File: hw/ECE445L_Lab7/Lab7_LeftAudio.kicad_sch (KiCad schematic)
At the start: 60 parts, among them Q10 PZT2222A, Q11 PZT2222A, Q12 PZT2222A, Q13 PZT2222A, Q14 PZT2222A, Q15 PZT2222A, Q16 PZT2222A, Q17 PZT2222A, Q18 PZT2222A, U11 OPA2350, U12 OPA2350, U13 OPA2350, U15 TLV5616, U6 OPA2350

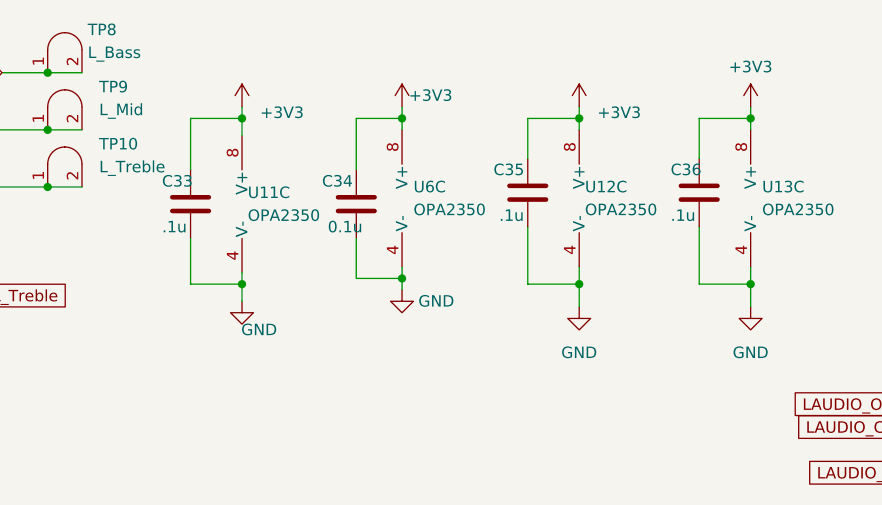
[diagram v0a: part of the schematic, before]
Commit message: Made changers to the schematic, updated bom, and created priliminary layout for the PCB. Ready for 7B Prep!
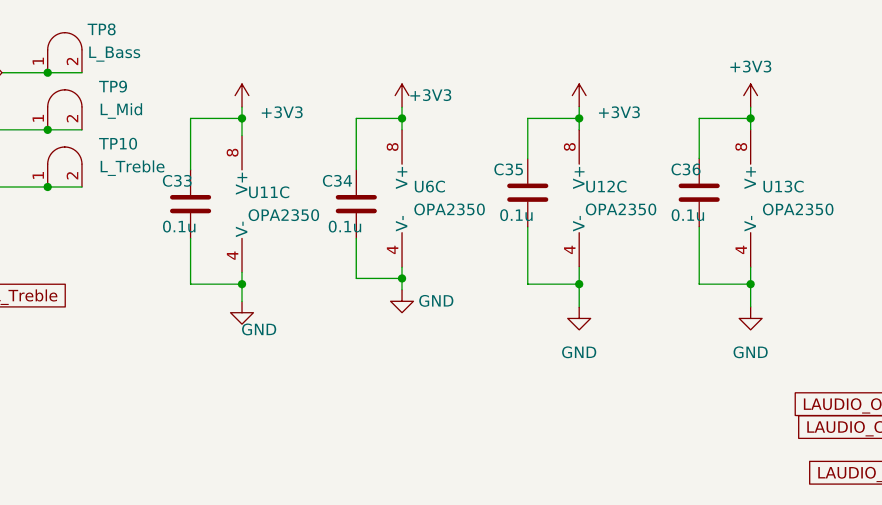
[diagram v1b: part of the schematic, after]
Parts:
- C27, C28, C29, C30, C31, C32, C34: footprint Capacitor_SMD:C_0805_2012Metric -> Capacitor_SMD:C_0603_1608Metric
- C33, C35, C36: value .1u -> 0.1u; footprint Capacitor_SMD:C_0805_2012Metric -> Capacitor_SMD:C_0603_1608Metric
- C37: footprint ECE445L:C_Axial_200mil -> Capacitor_SMD:C_0603_1608Metric
- R29, R30, R31, R32, R33, R34, R35, R36, R37, R38, R39, R40, R41, R42, R43, R44, R45, R46, R47, R48, R49, R50, R51, R52, R53, R54, R55, R56, R57: footprint Resistor_SMD:R_0805_2012Metric -> Resistor_SMD:R_0603_1608Metric
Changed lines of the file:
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@@
 			)
 		)
-		(property "Footprint" "Capacitor_SMD:C_0805_2012Metric"
+		(property "Footprint" "Capacitor_SMD:C_0603_1608Metric"
 			(at 42.545 37.7698 0)
 			(effects
@@
 			)
 		)
-		(property "Footprint" "Resistor_SMD:R_0805_2012Metric"
+		(property "Footprint" "Resistor_SMD:R_0603_1608Metric"
 			(at 50.292 170.815 90)
 			(effects
@@
 			)
 		)
-		(property "Footprint" "Capacitor_SMD:C_0805_2012Metric"
+		(property "Footprint" "Capacitor_SMD:C_0603_1608Metric"
 			(at 146.9898 29.845 0)
 			(effects
@@
 			)
 		)
-		(property "Footprint" "Resistor_SMD:R_0805_2012Metric"
+		(property "Footprint" "Resistor_SMD:R_0603_1608Metric"
 			(at 45.593 52.07 90)
 			(effects
@@
 			)
 		)
-		(property "Footprint" "Resistor_SMD:R_0805_2012Metric"
+		(property "Footprint" "Resistor_SMD:R_0603_1608Metric"
 			(at 245.237 151.13 90)
 			(effects
@@
 			)
 		)
-		(property "Footprint" "Resistor_SMD:R_0805_2012Metric"
+		(property "Footprint" "Resistor_SMD:R_0603_1608Metric"
 			(at 89.027 111.76 90)
 			(effects
@@
 			)
 		)
-		(property "Footprint" "Resistor_SMD:R_0805_2012Metric"
+		(property "Footprint" "Resistor_SMD:R_0603_1608Metric"
 			(at 173.355 124.333 90)
 			(effects
@@
 			)
 		)
-		(property "Value" ".1u"
+		(property "Value" "0.1u"
 			(at 126.365 36.195 0)
 			(effects
@@
 			)
 		)
-		(property "Footprint" "Capacitor_SMD:C_0805_2012Metric"
+		(property "Footprint" "Capacitor_SMD:C_0603_1608Metric"
 			(at 128.5748 29.845 0)
 			(effects
@@
 			)
 		)
-		(property "Footprint" "Resistor_SMD:R_0805_2012Metric"
+		(property "Footprint" "Resistor_SMD:R_0603_1608Metric"
 			(at 241.427 151.13 90)
 			(effects
@@
 			)
 		)
-		(property "Footprint" "Resistor_SMD:R_0805_2012Metric"
+		(property "Footprint" "Resistor_SMD:R_0603_1608Metric"
 			(at 39.37 154.178 90)
 			(effects
@@
 			)
 		)
-		(property "Footprint" "Resistor_SMD:R_0805_2012Metric"
+		(property "Footprint" "Resistor_SMD:R_0603_1608Metric"
 			(at 49.657 57.15 90)
 			(effects
@@
 			)
 		)
-		(property "Footprint" "Resistor_SMD:R_0805_2012Metric"
+		(property "Footprint" "Resistor_SMD:R_0603_1608Metric"
 			(at 45.593 33.655 90)
 			(effects
@@
 			)
 		)
-		(property "Footprint" "Resistor_SMD:R_0805_2012Metric"
+		(property "Footprint" "Resistor_SMD:R_0603_1608Metric"
 			(at 226.695 126.873 90)
 			(effects
@@
 			)
 		)
-		(property "Footprint" "Resistor_SMD:R_0805_2012Metric"
+		(property "Footprint" "Resistor_SMD:R_0603_1608Metric"
 			(at 67.31 166.243 90)
 			(effects
@@
 			)
 		)
-		(property "Footprint" "Resistor_SMD:R_0805_2012Metric"
+		(property "Footprint" "Resistor_SMD:R_0603_1608Metric"
 			(at 27.305 150.622 90)
 			(effects
@@
 			)
 		)
-		(property "Footprint" "Resistor_SMD:R_0805_2012Metric"
+		(property "Footprint" "Resistor_SMD:R_0603_1608Metric"
 			(at 60.198 170.815 90)
 			(effects
@@
 			)
 		)
-		(property "Footprint" "Resistor_SMD:R_0805_2012Metric"
+		(property "Footprint" "Resistor_SMD:R_0603_1608Metric"
 			(at 84.328 99.06 90)
 			(effects
@@
 			)
 		)
-		(property "Footprint" "Resistor_SMD:R_0805_2012Metric"
+		(property "Footprint" "Resistor_SMD:R_0603_1608Metric"
 			(at 231.775 111.252 90)
 			(effects
@@
 			)
 		)
-		(property "Footprint" "Resistor_SMD:R_0805_2012Metric"
+		(property "Footprint" "Resistor_SMD:R_0603_1608Metric"
 			(at 59.563 57.15 90)
 			(effects
@@
 			)
 		)
-		(property "Footprint" "Resistor_SMD:R_0805_2012Metric"
+		(property "Footprint" "Resistor_SMD:R_0603_1608Metric"
 			(at 226.568 106.68 90)
 			(effects
@@
 			)
 		)
-		(property "Footprint" "Resistor_SMD:R_0805_2012Metric"
+		(property "Footprint" "Resistor_SMD:R_0603_1608Metric"
 			(at 98.933 111.76 90)
 			(effects
@@
 			)
 		)
-		(property "Footprint" "Resistor_SMD:R_0805_2012Metric"
+		(property "Footprint" "Resistor_SMD:R_0603_1608Metric"
 			(at 268.097 151.13 90)
 			(effects
@@
 			)
 		)
-		(property "Footprint" "Resistor_SMD:R_0805_2012Metric"
+		(property "Footprint" "Resistor_SMD:R_0603_1608Metric"
 			(at 217.678 106.045 90)
 			(effects
@@
 			)
 		)
-		(property "Footprint" "Resistor_SMD:R_0805_2012Metric"
+		(property "Footprint" "Resistor_SMD:R_0603_1608Metric"
 			(at 256.032 151.13 90)
 			(effects
@@
 			)
 		)
-		(property "Footprint" "ECE445L:C_Axial_200mil"
+		(property "Footprint" "Capacitor_SMD:C_0603_1608Metric"
 			(at 261.9502 52.07 0)
 			(effects
@@
 			)
 		)
-		(property "Footprint" "Resistor_SMD:R_0805_2012Metric"
+		(property "Footprint" "Resistor_SMD:R_0603_1608Metric"
 			(at 106.045 107.188 90)
 			(effects
@@
 			)
 		)
-		(property "Footprint" "Resistor_SMD:R_0805_2012Metric"
+		(property "Footprint" "Resistor_SMD:R_0603_1608Metric"
 			(at 66.675 52.578 90)
 			(effects
@@
 			)
 		)
-		(property "Footprint" "Resistor_SMD:R_0805_2012Metric"
+		(property "Footprint" "Resistor_SMD:R_0603_1608Metric"
 			(at 173.355 135.128 90)
 			(effects
@@
 			)
 		)
-		(property "Footprint" "Resistor_SMD:R_0805_2012Metric"
+		(property "Footprint" "Resistor_SMD:R_0603_1608Metric"
 			(at 29.972 27.94 90)
 			(effects
@@
 			)
 		)
-		(property "Footprint" "Capacitor_SMD:C_0805_2012Metric"
+		(property "Footprint" "Capacitor_SMD:C_0603_1608Metric"
 			(at 124.1298 98.425 0)
 			(effects
@@
 			)
 		)
-		(property "Value" ".1u"
+		(property "Value" "0.1u"
 			(at 163.83 34.925 0)
 			(effects
@@
 			)
 		)
-		(property "Footprint" "Capacitor_SMD:C_0805_2012Metric"
+		(property "Footprint" "Capacitor_SMD:C_0603_1608Metric"
 			(at 166.0398 28.575 0)
 			(effects
@@
 			)
 		)
-		(property "Footprint" "Capacitor_SMD:C_0805_2012Metric"
+		(property "Footprint" "Capacitor_SMD:C_0603_1608Metric"
 			(at 30.48 37.7698 0)
 			(effects
@@
 			)
 		)
-		(property "Footprint" "Capacitor_SMD:C_0805_2012Metric"
+		(property "Footprint" "Capacitor_SMD:C_0603_1608Metric"
 			(at 78.74 91.7448 0)
 			(effects
@@
 			)
 		)
-		(property "Footprint" "Resistor_SMD:R_0805_2012Metric"
+		(property "Footprint" "Resistor_SMD:R_0603_1608Metric"
 			(at 173.99 113.538 90)
 			(effects
@@
 			)
 		)
-		(property "Footprint" "Capacitor_SMD:C_0805_2012Metric"
+		(property "Footprint" "Capacitor_SMD:C_0603_1608Metric"
 			(at 34.6202 147.32 0)
 			(effects
@@
 			)
 		)
-		(property "Footprint" "Resistor_SMD:R_0805_2012Metric"
+		(property "Footprint" "Resistor_SMD:R_0603_1608Metric"
 			(at 84.328 87.63 90)
 			(effects
@@
 			)
 		)
-		(property "Footprint" "Resistor_SMD:R_0805_2012Metric"
+		(property "Footprint" "Resistor_SMD:R_0603_1608Metric"
 			(at 117.475 97.028 90)
 			(effects
@@
 			)
 		)
-		(property "Footprint" "Resistor_SMD:R_0805_2012Metric"
+		(property "Footprint" "Resistor_SMD:R_0603_1608Metric"
 			(at 217.678 135.255 90)
 			(effects
@@
 			)
 		)
-		(property "Value" ".1u"
+		(property "Value" "0.1u"
 			(at 182.88 34.925 0)
 			(effects
@@
 			)
 		)
-		(property "Footprint" "Capacitor_SMD:C_0805_2012Metric"
+		(property "Footprint" "Capacitor_SMD:C_0603_1608Metric"
 			(at 185.0898 28.575 0)
 			(effects
@@
 			)
 		)
-		(property "Footprint" "Capacitor_SMD:C_0805_2012Metric"
+		(property "Footprint" "Capacitor_SMD:C_0603_1608Metric"
 			(at 45.4152 169.545 0)
 			(effects

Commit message: Rough draft layout - need to remove tm4c chip
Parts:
- removed TP10: L_Treble, ECE445L:Testpoint_1x02_P2.54mm, symbol ECE445L:Testpoint
- removed TP11: L_Buff, ECE445L:Testpoint_1x02_P2.54mm, symbol ECE445L:Testpoint
- removed TP12: L_Out, ECE445L:Testpoint_1x02_P2.54mm, symbol ECE445L:Testpoint
- removed TP8: L_Bass, ECE445L:Testpoint_1x02_P2.54mm, symbol ECE445L:Testpoint
- removed TP9: L_Mid, ECE445L:Testpoint_1x02_P2.54mm, symbol ECE445L:Testpoint
- added R59: 40k, Resistor_SMD:R_0603_1608Metric_Pad0.98x0.95mm_HandSolder, symbol Device:R
- added R60: 3.3k, Resistor_SMD:R_0603_1608Metric_Pad0.98x0.95mm_HandSolder, symbol Device:R
- C27: renamed from C31; footprint Capacitor_SMD:C_0603_1608Metric -> Capacitor_SMD:C_0603_1608Metric_Pad1.08x0.95mm_HandSolder
- C28: renamed from C27; value 27n -> 30n; footprint Capacitor_SMD:C_0603_1608Metric -> Capacitor_SMD:C_0603_1608Metric_Pad1.08x0.95mm_HandSolder
- C29: renamed from C32; footprint Capacitor_SMD:C_0603_1608Metric -> Capacitor_SMD:C_0603_1608Metric_Pad1.08x0.95mm_HandSolder
- C30: renamed from C28; value 27n -> 30n; footprint Capacitor_SMD:C_0603_1608Metric -> Capacitor_SMD:C_0603_1608Metric_Pad1.08x0.95mm_HandSolder
- C31: renamed from C29; value 10n -> 9.5n; footprint Capacitor_SMD:C_0603_1608Metric -> Capacitor_SMD:C_0603_1608Metric_Pad1.08x0.95mm_HandSolder
- C32: renamed from C30; value 3.5n -> 3.7n; footprint Capacitor_SMD:C_0603_1608Metric -> Capacitor_SMD:C_0603_1608Metric_Pad1.08x0.95mm_HandSolder
- C33, C34, C35, C36: footprint Capacitor_SMD:C_0603_1608Metric -> Capacitor_SMD:C_0603_1608Metric_Pad1.08x0.95mm_HandSolder
- C37: renamed from C40; footprint Capacitor_SMD:C_0805_2012Metric -> Capacitor_SMD:C_0805_2012Metric_Pad1.18x1.45mm_HandSolder
- C38: renamed from C37; footprint Capacitor_SMD:C_0603_1608Metric -> Capacitor_SMD:C_0603_1608Metric_Pad1.08x0.95mm_HandSolder
- R39: renamed from R29; footprint Resistor_SMD:R_0603_1608Metric -> Resistor_SMD:R_0603_1608Metric_Pad0.98x0.95mm_HandSolder
- R40: footprint Resistor_SMD:R_0603_1608Metric -> Resistor_SMD:R_0603_1608Metric_Pad0.98x0.95mm_HandSolder
- R41: renamed from R30; footprint Resistor_SMD:R_0603_1608Metric -> Resistor_SMD:R_0603_1608Metric_Pad0.98x0.95mm_HandSolder
- R42: renamed from R43; footprint Resistor_SMD:R_0603_1608Metric -> Resistor_SMD:R_0603_1608Metric_Pad0.98x0.95mm_HandSolder
- R43: renamed from R44; footprint Resistor_SMD:R_0603_1608Metric -> Resistor_SMD:R_0603_1608Metric_Pad0.98x0.95mm_HandSolder
- R44: renamed from R45; footprint Resistor_SMD:R_0603_1608Metric -> Resistor_SMD:R_0603_1608Metric_Pad0.98x0.95mm_HandSolder
- R45: renamed from R33; footprint Resistor_SMD:R_0603_1608Metric -> Resistor_SMD:R_0603_1608Metric_Pad0.98x0.95mm_HandSolder
- R46: renamed from R42; footprint Resistor_SMD:R_0603_1608Metric -> Resistor_SMD:R_0603_1608Metric_Pad0.98x0.95mm_HandSolder
- R47: renamed from R32; footprint Resistor_SMD:R_0603_1608Metric -> Resistor_SMD:R_0603_1608Metric_Pad0.98x0.95mm_HandSolder
- R48: renamed from R41; footprint Resistor_SMD:R_0603_1608Metric -> Resistor_SMD:R_0603_1608Metric_Pad0.98x0.95mm_HandSolder
- R49: renamed from R31; footprint Resistor_SMD:R_0603_1608Metric -> Resistor_SMD:R_0603_1608Metric_Pad0.98x0.95mm_HandSolder
- R50: renamed from R34; footprint Resistor_SMD:R_0603_1608Metric -> Resistor_SMD:R_0603_1608Metric_Pad0.98x0.95mm_HandSolder
- R51: renamed from R35; footprint Resistor_SMD:R_0603_1608Metric -> Resistor_SMD:R_0603_1608Metric_Pad0.98x0.95mm_HandSolder
- R52: renamed from R39; footprint Resistor_SMD:R_0603_1608Metric -> Resistor_SMD:R_0603_1608Metric_Pad0.98x0.95mm_HandSolder
- R53: renamed from R38; footprint Resistor_SMD:R_0603_1608Metric -> Resistor_SMD:R_0603_1608Metric_Pad0.98x0.95mm_HandSolder
- R54: renamed from R37; footprint Resistor_SMD:R_0603_1608Metric -> Resistor_SMD:R_0603_1608Metric_Pad0.98x0.95mm_HandSolder
- R55: renamed from R36; footprint Resistor_SMD:R_0603_1608Metric -> Resistor_SMD:R_0603_1608Metric_Pad0.98x0.95mm_HandSolder
- R56: renamed from R47; value 10k -> 7.5k; footprint Resistor_SMD:R_0603_1608Metric -> Resistor_SMD:R_0603_1608Metric_Pad0.98x0.95mm_HandSolder
- R57: renamed from R48; footprint Resistor_SMD:R_0603_1608Metric -> Resistor_SMD:R_0603_1608Metric_Pad0.98x0.95mm_HandSolder
- R58: renamed from R46; footprint Resistor_SMD:R_0603_1608Metric -> Resistor_SMD:R_0603_1608Metric_Pad0.98x0.95mm_HandSolder
- R61: renamed from R49; footprint Resistor_SMD:R_0603_1608Metric -> Resistor_SMD:R_0603_1608Metric_Pad0.98x0.95mm_HandSolder
- R62: renamed from R50; footprint Resistor_SMD:R_0603_1608Metric -> Resistor_SMD:R_0603_1608Metric_Pad0.98x0.95mm_HandSolder
- R63: renamed from R52; footprint Resistor_SMD:R_0603_1608Metric -> Resistor_SMD:R_0603_1608Metric_Pad0.98x0.95mm_HandSolder
- R64: renamed from R51; footprint Resistor_SMD:R_0603_1608Metric -> Resistor_SMD:R_0603_1608Metric_Pad0.98x0.95mm_HandSolder
- R65: renamed from R53; footprint Resistor_SMD:R_0603_1608Metric -> Resistor_SMD:R_0603_1608Metric_Pad0.98x0.95mm_HandSolder
- R66: renamed from R54; footprint Resistor_SMD:R_0603_1608Metric -> Resistor_SMD:R_0603_1608Metric_Pad0.98x0.95mm_HandSolder
- R67: renamed from R55; footprint Resistor_SMD:R_0603_1608Metric -> Resistor_SMD:R_0603_1608Metric_Pad0.98x0.95mm_HandSolder
- R68: renamed from R57; footprint Resistor_SMD:R_0603_1608Metric -> Resistor_SMD:R_0603_1608Metric_Pad0.98x0.95mm_HandSolder
- R69: renamed from R56; footprint Resistor_SMD:R_0603_1608Metric -> Resistor_SMD:R_0603_1608Metric_Pad0.98x0.95mm_HandSolder
- renumbered U6 to U11, U6 to U12, U11 to U12, U12 to U13, U13 to U14
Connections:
- net R_Bass is gone; now on net L_Bass: R57.1
- net R_Mid is gone; now on net L_Mid: R56.1
- net R_Treble is gone; now on net L_Treble: R58.1
- net Vin is gone; now on net Vin_L: C27.1, C31.1
- net GND: now also R65.2, R59.1; no longer R65.1
- net L_Buff: now also R60.2; no longer U14.2 (-)
- net Vin_L: now also R39.1; no longer R39.2
- net at C28.2, R41.1: now also R39.2; no longer R39.1
- net at R50.1, R51.2: now also C31.2, U13.3 (+)
- net at R63.1, U14.5 (+): now also R65.1; no longer R65.2
- new net: R59.2, R60.1, U14.2 (-)
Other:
- company: (none) -> The University of Texas at Austin
- title: (none) -> ECE 445L Lab7
- moved on the sheet: R39, R65, U12B

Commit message: Added current consumption to schematic
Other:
- note added: "100k Ohm Resistor Dividers : 2 * (0.0165 mA) = 0.033 mA 200k Ohm Resistor Dividers : 1 * 0.00825 = 0.00825 mA 10k Ohm Resitor Dividers : 3 * (0.165 mA) = 0.5 mA 75k Ohm Loads : 1 * (0.044 mA) = 0.044 mA OPA2350s : 8 * (7.5 mA) = 60 mA TLV5616s : 1 * (1.1mA) = 1.1 mA Total : 61.6825 mA"
- note added: "Current per 100k Ohm Resitor Divider +3V3 / (100k + 100k) = 0.0165 mA Current per 200k Ohm Resistor Divider +3V3 / (200k + 200k) = 0.00825 mA Current per 10k Ohm Resitor Divider +3V3 / (10k + 10k) = 0.165 mA Current per 75k Load +3V3 / 75k = 0.044 mA Quiescent Current (Per Amplifier - 2x per chip) 7.5 mA Current Per TLV5616 1.1 mA"
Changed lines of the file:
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@@
+		)
+	)
+	(text "100k Ohm Resistor Dividers : 2 * (0.0165 mA) = 0.033 mA\n200k Ohm Resistor Dividers : 1 * 0.00825 = 0.00825 mA\n10k Ohm Resitor Dividers : 3 * (0.165 mA) = 0.5 mA\n75k Ohm Loads : 1 * (0.044 mA) = 0.044 mA\nOPA2350s : 8 * (7.5 mA) = 60 mA\nTLV5616s : 1 * (1.1mA) = 1.1 mA\n\nTotal : 61.6825 mA"
+		(exclude_from_sim no)
+		(at 117.475 185.42 0)
+		(effects
+			(font
+				(size 1.27 1.27)
+			)
+			(justify left)
 		)
 	)
@@
 		)
 	)
+	(text "Current per 100k Ohm Resitor Divider\n+3V3 / (100k + 100k) = 0.0165 mA\n\nCurrent per 200k Ohm Resistor Divider\n+3V3 / (200k + 200k) = 0.00825 mA\n\nCurrent per 10k Ohm Resitor Divider\n+3V3 / (10k + 10k) = 0.165 mA\n\nCurrent per 75k Load\n+3V3 / 75k = 0.044 mA\n\nQuiescent Current (Per Amplifier - 2x per chip)\n7.5 mA\n\nCurrent Per TLV5616\n1.1 mA\n"
+		(exclude_from_sim no)
+		(at 118.11 156.845 0)
+		(effects
+			(font
+				(size 1.27 1.27)
+			)
+			(justify left)
+		)
+	)

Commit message: Updated lab7a report
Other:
- note added: "Left Audio Current Consumption : Current per 100k Ohm Resitor Divider +3V3 / (100k + 100k) = 0.0165 mA Current per 200k Ohm Resistor Divider +3V3 / (200k + 200k) = 0.00825 mA Current per 10k Ohm Resitor Divider +3V3 / (10k + 10k) = 0.165 mA Current per 75k Load +3V3 / 75k = 0.044 mA Quiescent Current (Per Amplifier - 2x per chip) 7.5 mA Current Per TLV5616 1.1 mA"
- note removed: "Current per 100k Ohm Resitor Divider +3V3 / (100k + 100k) = 0.0165 mA Current per 200k Ohm Resistor Divider +3V3 / (200k + 200k) = 0.00825 mA Current per 10k Ohm Resitor Divider +3V3 / (10k + 10k) = 0.165 mA Current per 75k Load +3V3 / 75k = 0.044 mA Quiescent Current (Per Amplifier - 2x per chip) 7.5 mA Current Per TLV5616 1.1 mA"
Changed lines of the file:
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@@
 		)
 	)
-	(text "Current per 100k Ohm Resitor Divider\n+3V3 / (100k + 100k) = 0.0165 mA\n\nCurrent per 200k Ohm Resistor Divider\n+3V3 / (200k + 200k) = 0.00825 mA\n\nCurrent per 10k Ohm Resitor Divider\n+3V3 / (10k + 10k) = 0.165 mA\n\nCurrent per 75k Load\n+3V3 / 75k = 0.044 mA\n\nQuiescent Current (Per Amplifier - 2x per chip)\n7.5 mA\n\nCurrent Per TLV5616\n1.1 mA\n"
+	(text "Left Audio Current Consumption :\n\nCurrent per 100k Ohm Resitor Divider\n+3V3 / (100k + 100k) = 0.0165 mA\n\nCurrent per 200k Ohm Resistor Divider\n+3V3 / (200k + 200k) = 0.00825 mA\n\nCurrent per 10k Ohm Resitor Divider\n+3V3 / (10k + 10k) = 0.165 mA\n\nCurrent per 75k Load\n+3V3 / 75k = 0.044 mA\n\nQuiescent Current (Per Amplifier - 2x per chip)\n7.5 mA\n\nCurrent Per TLV5616\n1.1 mA\n"
 		(exclude_from_sim no)
 		(at 118.11 156.845 0)

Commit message: PCB Layout
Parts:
- added R105, R106, R107, R108, R109, R110, R111, R112, R113: 2k, Resistor_SMD:R_0603_1608Metric_Pad0.98x0.95mm_HandSolder, symbol Device:R
- added TP10: L_Bass, ECE445L:Testpoint_1x02_P2.54mm, symbol ECE445L:Testpoint
- added TP8: L_Treble, ECE445L:Testpoint_1x02_P2.54mm, symbol ECE445L:Testpoint
- added TP9: L_Mid, ECE445L:Testpoint_1x02_P2.54mm, symbol ECE445L:Testpoint
- Q10, Q11, Q12, Q13, Q14, Q15, Q16, Q17, Q18: value PZT2222A -> MMBF170; footprint Package_TO_SOT_SMD:SOT-223-3_TabPin2 -> Package_TO_SOT_SMD:SOT-23-3
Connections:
- net L_Bass: now also TP10.1 (A), TP10.2 (B)
- net L_Mid: now also TP9.1 (A), TP9.2 (B)
- net L_Treble: now also TP8.1 (A), TP8.2 (B)
- net PB2: now also R107.1; no longer Q11.1 (B)
- net PB3: now also R108.2; no longer Q13.1 (B)
- net PB4: now also R105.1; no longer Q14.1 (B)
- net PB5: now also R106.2; no longer Q15.1 (B)
- net PB6: now also R109.1; no longer Q10.1 (B)
- net PB7: now also R110.2; no longer Q12.1 (B)
- net PC4: now also R111.2; no longer Q16.1 (B)
- net PC5: now also R112.1; no longer Q17.1 (B)
- net PC6: now also R113.1; no longer Q18.1 (B)
- net at R45.1, R49.1, U12.2 (-): now also R47.1; no longer R47.2
- net at R52.1, R54.1, U13.2 (-): now also R53.1; no longer R53.2
- net at Q12.2 (C): now also R46.2; no longer R46.1
- net at R44.1, R48.1, U11.2 (-): now also R46.1; no longer R46.2
- net at Q13.2 (C): now also R47.2; no longer R47.1
- net at Q15.2 (C): now also R53.2; no longer R53.1
- new net: Q14.1 (B), R105.2
- new net: Q12.1 (B), R110.1
- new net: Q11.1 (B), R107.2
- new net: Q10.1 (B), R109.2
- new net: Q18.1 (B), R113.2
- new net: Q17.1 (B), R112.2
- new net: Q16.1 (B), R111.1
- new net: Q13.1 (B), R108.1
- new net: Q15.1 (B), R106.1
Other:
- moved on the sheet: R46, R47, R53

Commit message: Pushing so i can work on my desktop
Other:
- note added: "Changed To MOSFETs (Had wrong part number)"
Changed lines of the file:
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@@
+		)
+	)
+	(text "Changed To MOSFETs\n(Had wrong part number)"
+		(exclude_from_sim no)
+		(at 269.875 161.925 0)
+		(effects
+			(font
+				(size 1.27 1.27)
+			)
 		)
 	)
@@
 		)
 	)
+	(text "Changed To MOSFETs\n(Had wrong part number)"
+		(exclude_from_sim no)
+		(at 71.12 192.405 0)
+		(effects
+			(font
+				(size 1.27 1.27)
+			)
+		)
+	)
+	(text "Changed To MOSFETs\n(Had wrong part number)"
+		(exclude_from_sim no)
+		(at 109.855 129.54 0)
+		(effects
+			(font
+				(size 1.27 1.27)
+			)
+		)
+	)
 	(text "Variable Gain"
 		(exclude_from_sim no)
@@
 		(effects
 			(font
+				(size 1.27 1.27)
+			)
+		)
+	)
+	(text "Changed To MOSFETs\n(Had wrong part number)"
+		(exclude_from_sim no)
+		(at 36.83 78.74 0)
+		(effects
+			(font
